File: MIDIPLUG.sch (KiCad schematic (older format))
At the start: 33 parts, among them P1 LINE OUT, U1 LP2985-3.3, U2 SAM2695, Y1 12Mhz

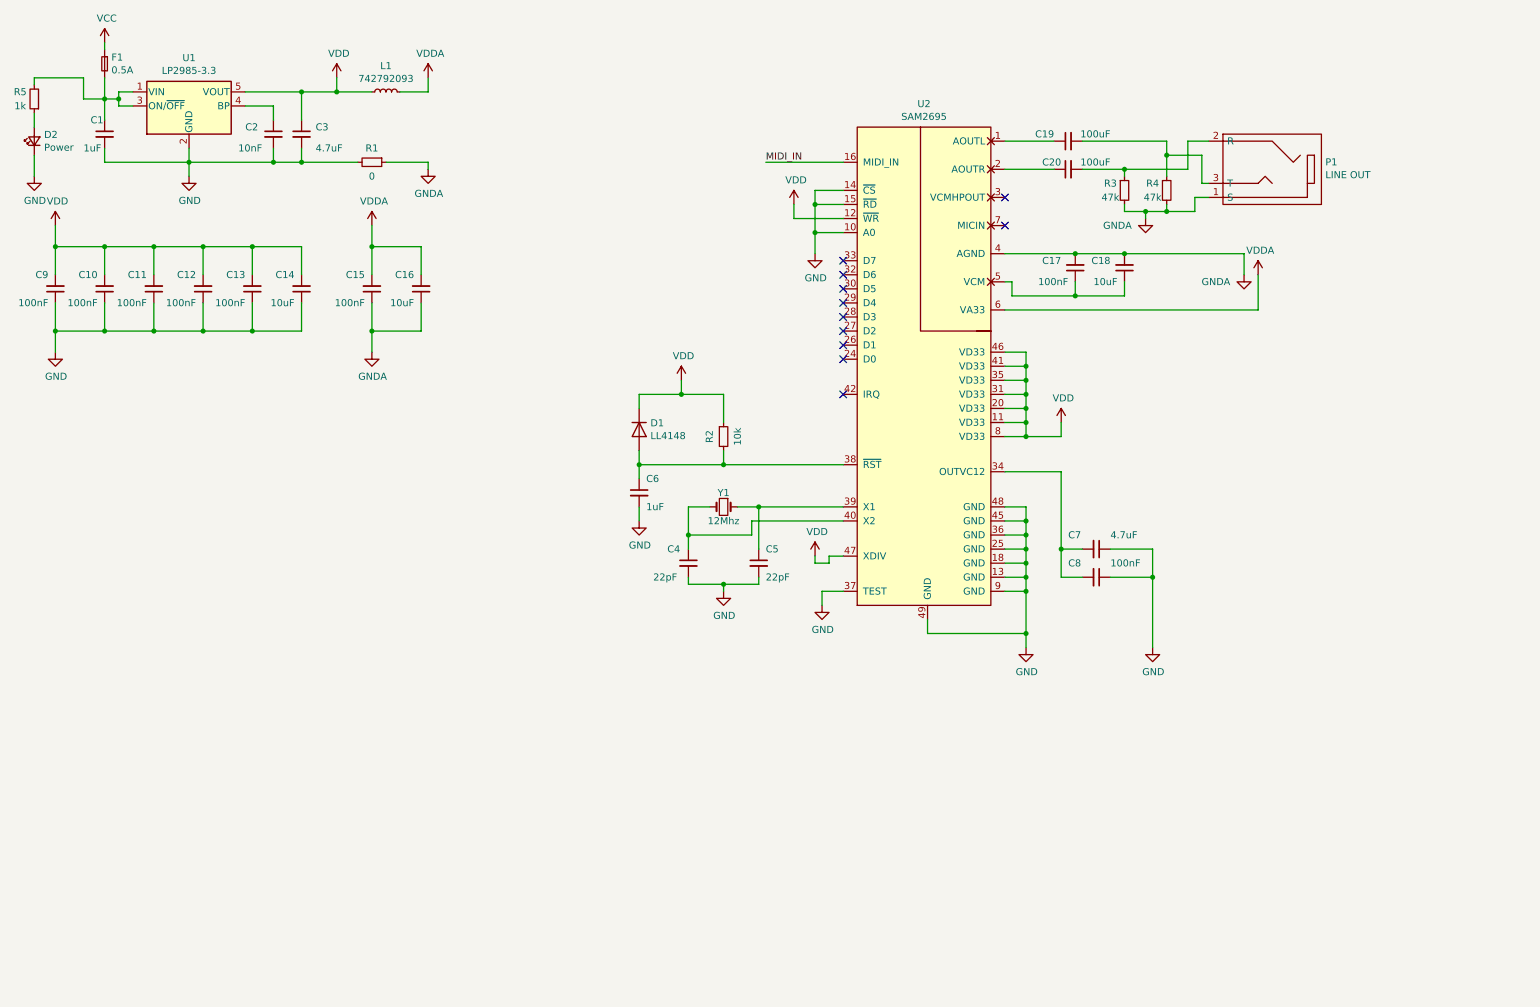
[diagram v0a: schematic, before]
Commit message: Add joystick plug
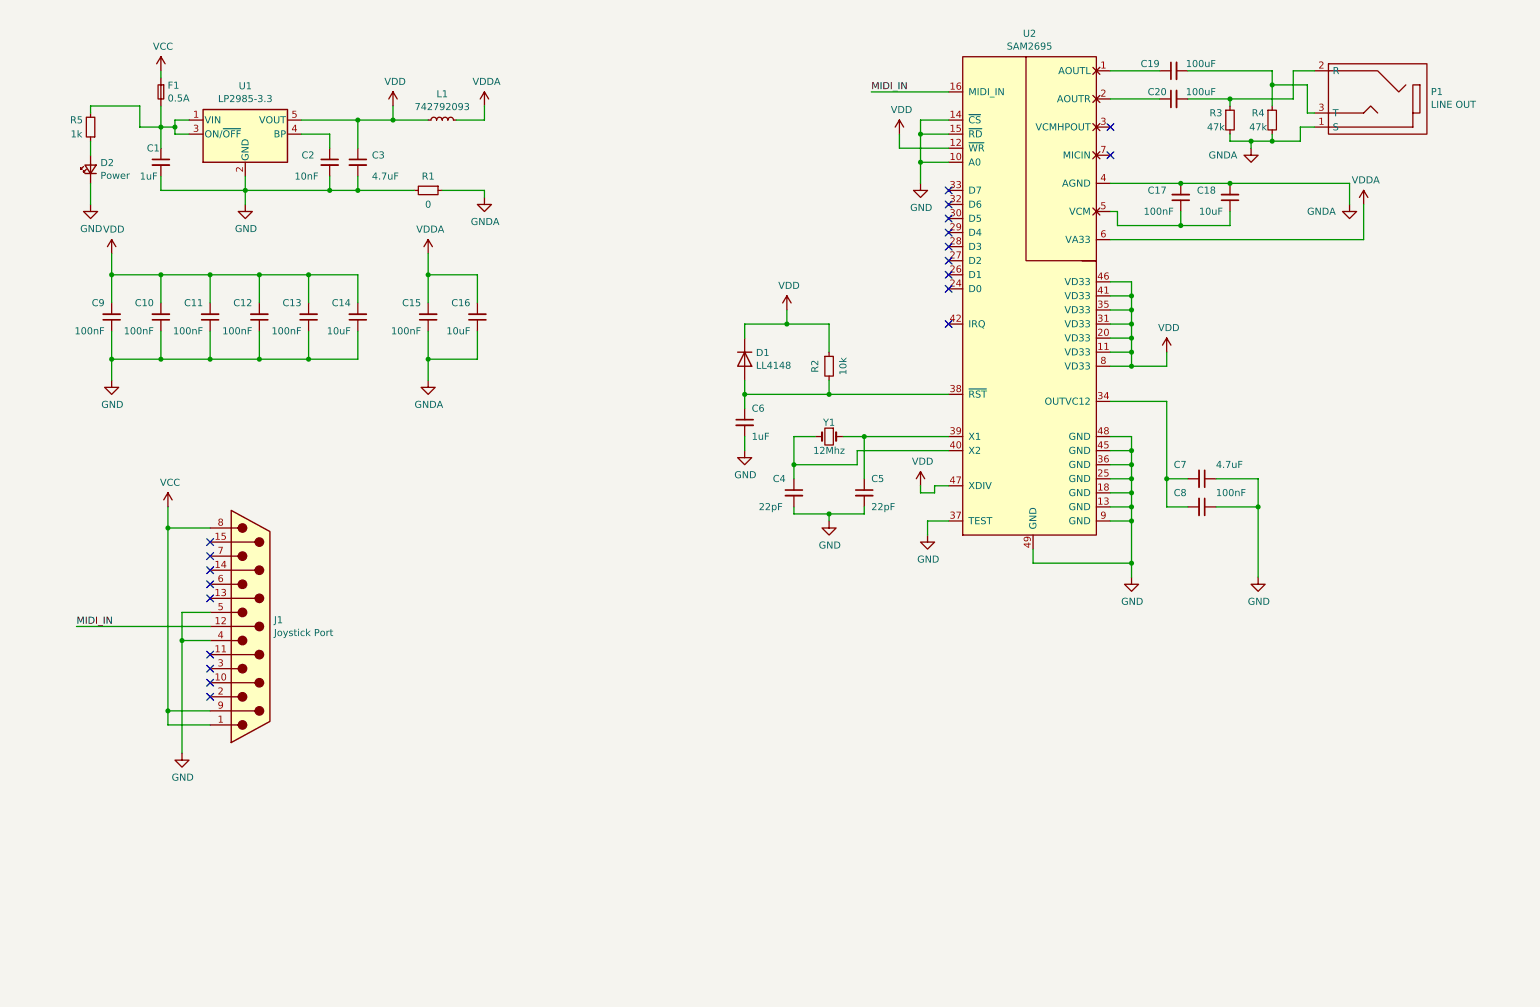
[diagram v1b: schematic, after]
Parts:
- added J1: Joystick Port, symbol Connector:DB15_Male
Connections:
- net GND: now also J1.4, J1.5
- net MIDI_IN: now also J1.12 (P12)
- net VCC: now also J1.1, J1.8, J1.9 (P9)
- no-connect marks 11 -> 20
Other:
- moved on the sheet: C1, C10, C11, C12, C13, C14, C15, C16, C17, C18, C19, C2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

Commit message: Begin placing components
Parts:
- C1: footprint (none) -> Capacitor_SMD:C_0805_2012Metric_Pad1.18x1.45mm_HandSolder
- C19, C20: footprint (none) -> Capacitor_SMD:C_1206_3216Metric_Pad1.33x1.80mm_HandSolder
- D2: footprint (none) -> LED_SMD:LED_1206_3216Metric_Pad1.42x1.75mm_HandSolder
- F1: footprint (none) -> Fuse:Fuse_1206_3216Metric_Pad1.42x1.75mm_HandSolder
- J1: footprint (none) -> Connector_Dsub:DSUB-15_Male_EdgeMount_P2.77mm
- L1: footprint (none) -> Inductor_SMD:L_0805_2012Metric_Pad1.15x1.40mm_HandSolder
- P1: footprint (none) -> My_Components:Conn_Audio_3.5mm_Stereo_SJ1-352XNG
- R1, R2, R3, R4, R5: footprint (none) -> Resistor_SMD:R_0805_2012Metric_Pad1.20x1.40mm_HandSolder
- U2: footprint (none) -> Package_DFN_QFN:QFN-48-1EP_6x6mm_P0.4mm_EP4.3x4.3mm_ThermalVias
- Y1: footprint (none) -> Crystal:Crystal_SMD_HC49-SD

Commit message: First version of the PCB
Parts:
- removed C11, C12, C13: 100nF, symbol Device:C_Small
- C10, C14, C15, C16, C17, C18, C2, C3, C4, C5, C6, C7, C8, C9: footprint (none) -> Capacitor_SMD:C_0805_2012Metric_Pad1.18x1.45mm_HandSolder
- D2: footprint LED_SMD:LED_1206_3216Metric_Pad1.42x1.75mm_HandSolder -> LED_SMD:LED_0805_2012Metric_Pad1.15x1.40mm_HandSolder
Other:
- moved on the sheet: C14, C4, C5
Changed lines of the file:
@@
 F 0 "C2" H 2600 1800 50  0000 L CNN
 F 1 "10nF" H 2550 1650 50  0000 L CNN
-F 2 "" H 2800 1750 50  0001 C CNN
+F 2 "Capacitor_SMD:C_0805_2012Metric_Pad1.18x1.45mm_HandSolder" H 2800 1750 50  0001 C CNN
 F 3 "~" H 2800 1750 50  0001 C CNN
 	1    2800 1750
@@
 F 0 "C3" H 3100 1800 50  0000 L CNN
 F 1 "4.7uF" H 3100 1650 50  0000 L CNN
-F 2 "" H 3000 1750 50  0001 C CNN
+F 2 "Capacitor_SMD:C_0805_2012Metric_Pad1.18x1.45mm_HandSolder" H 3000 1750 50  0001 C CNN
 F 3 "~" H 3000 1750 50  0001 C CNN
 	1    3000 1750
@@
 	8500 4700 8500 4600
 Connection ~ 8500 4600
-$Comp
-L Device:Crystal_Small Y1
-U 1 1 60B4BC85
-P 6350 3700
-F 0 "Y1" H 6350 3600 50  0000 C CNN
-F 1 "12Mhz" H 6350 3800 50  0000 C CNN
-F 2 "Crystal:Crystal_SMD_HC49-SD" H 6350 3700 50  0001 C CNN
-F 3 "~" H 6350 3700 50  0001 C CNN
-	1    6350 3700
-	-1   0    0    1
-$EndComp
-$Comp
-L Device:C_Small C4
-U 1 1 60B4CDD2
-P 6100 4100
-F 0 "C4" H 5950 4200 50  0000 L CNN
-F 1 "22pF" H 5850 4000 50  0000 L CNN
-F 2 "" H 6100 4100 50  0001 C CNN
-F 3 "~" H 6100 4100 50  0001 C CNN
-	1    6100 4100
-	1    0    0    -1
-$EndComp
-$Comp
-L Device:C_Small C5
-U 1 1 60B4E9FB
-P 6600 4100
-F 0 "C5" H 6650 4200 50  0000 L CNN
-F 1 "22pF" H 6650 4000 50  0000 L CNN
-F 2 "" H 6600 4100 50  0001 C CNN
-F 3 "~" H 6600 4100 50  0001 C CNN
-	1    6600 4100
-	1    0    0    -1
-$EndComp
 Wire Wire Line
 	7200 1750 7000 1750
@@
 F 0 "C6" H 5800 3700 50  0000 L CNN
 F 1 "1uF" H 5800 3500 50  0000 L CNN
-F 2 "" H 5750 3600 50  0001 C CNN
+F 2 "Capacitor_SMD:C_0805_2012Metric_Pad1.18x1.45mm_HandSolder" H 5750 3600 50  0001 C CNN
 F 3 "~" H 5750 3600 50  0001 C CNN
 	1    5750 3600
@@
 F 0 "C7" V 8900 3800 50  0000 L CNN
 F 1 "4.7uF" V 8900 4100 50  0000 L CNN
-F 2 "" H 9000 4000 50  0001 C CNN
+F 2 "Capacitor_SMD:C_0805_2012Metric_Pad1.18x1.45mm_HandSolder" H 9000 4000 50  0001 C CNN
 F 3 "~" H 9000 4000 50  0001 C CNN
 	1    9000 4000
@@
 F 0 "C8" V 8900 4000 50  0000 L CNN
 F 1 "100nF" V 8900 4300 50  0000 L CNN
-F 2 "" H 9000 4200 50  0001 C CNN
+F 2 "Capacitor_SMD:C_0805_2012Metric_Pad1.18x1.45mm_HandSolder" H 9000 4200 50  0001 C CNN
 F 3 "~" H 9000 4200 50  0001 C CNN
 	1    9000 4200
@@
 F 0 "C9" H 1300 2750 50  0000 L CNN
 F 1 "100nF" H 1300 2950 50  0000 L CNN
-F 2 "" H 1250 2850 50  0001 C CNN
+F 2 "Capacitor_SMD:C_0805_2012Metric_Pad1.18x1.45mm_HandSolder" H 1250 2850 50  0001 C CNN
 F 3 "~" H 1250 2850 50  0001 C CNN
 	1    1250 2850
@@
 F 0 "C10" H 1650 2750 50  0000 L CNN
 F 1 "100nF" H 1650 2950 50  0000 L CNN
-F 2 "" H 1600 2850 50  0001 C CNN
+F 2 "Capacitor_SMD:C_0805_2012Metric_Pad1.18x1.45mm_HandSolder" H 1600 2850 50  0001 C CNN
 F 3 "~" H 1600 2850 50  0001 C CNN
 	1    1600 2850
@@
 $EndComp
 $Comp
-L Device:C_Small C11
-U 1 1 60B93414
+L Device:C_Small C14
+U 1 1 60B967FC
 P 1950 2850
-F 0 "C11" H 2000 2750 50  0000 L CNN
-F 1 "100nF" H 2000 2950 50  0000 L CNN
-F 2 "" H 1950 2850 50  0001 C CNN
+F 0 "C14" H 2000 2750 50  0000 L CNN
+F 1 "10uF" H 2000 2950 50  0000 L CNN
+F 2 "Capacitor_SMD:C_0805_2012Metric_Pad1.18x1.45mm_HandSolder" H 1950 2850 50  0001 C CNN
 F 3 "~" H 1950 2850 50  0001 C CNN
 	1    1950 2850
 	-1   0    0    1
 $EndComp
-$Comp
-L Device:C_Small C12
-U 1 1 60B96526
-P 2300 2850
-F 0 "C12" H 2350 2750 50  0000 L CNN
-F 1 "100nF" H 2350 2950 50  0000 L CNN
-F 2 "" H 2300 2850 50  0001 C CNN
-F 3 "~" H 2300 2850 50  0001 C CNN
-	1    2300 2850
-	-1   0    0    1
-$EndComp
-$Comp
-L Device:C_Small C13
-U 1 1 60B967F2
-P 2650 2850
-F 0 "C13" H 2700 2750 50  0000 L CNN
-F 1 "100nF" H 2700 2950 50  0000 L CNN
-F 2 "" H 2650 2850 50  0001 C CNN
-F 3 "~" H 2650 2850 50  0001 C CNN
-	1    2650 2850
-	-1   0    0    1
-$EndComp
-$Comp
-L Device:C_Small C14
-U 1 1 60B967FC
-P 3000 2850
-F 0 "C14" H 3050 2750 50  0000 L CNN
-F 1 "10uF" H 3050 2950 50  0000 L CNN
-F 2 "" H 3000 2850 50  0001 C CNN
-F 3 "~" H 3000 2850 50  0001 C CNN
-	1    3000 2850
-	-1   0    0    1
-$EndComp
 Wire Wire Line
 	1250 2950 1250 3150
@@
 	1250 3150 1600 3150
 Wire Wire Line
-	3000 3150 3000 2950
-Wire Wire Line
-	2650 2950 2650 3150
-Connection ~ 2650 3150
-Wire Wire Line
-	2650 3150 3000 3150
-Wire Wire Line
-	2300 2950 2300 3150
-Connection ~ 2300 3150
-Wire Wire Line
-	2300 3150 2650 3150
-Wire Wire Line
 	1950 2950 1950 3150
-Connection ~ 1950 3150
-Wire Wire Line
-	1950 3150 2300 3150
 Wire Wire Line
 	1600 2950 1600 3150
@@
 	1250 2550 1600 2550
 Wire Wire Line
-	3000 2550 3000 2750
-Wire Wire Line
-	2650 2750 2650 2550
-Connection ~ 2650 2550
-Wire Wire Line
-	2650 2550 3000 2550
-Wire Wire Line
-	2300 2750 2300 2550
-Connection ~ 2300 2550
-Wire Wire Line
-	2300 2550 2650 2550
-Wire Wire Line
 	1950 2750 1950 2550
-Connection ~ 1950 2550
-Wire Wire Line
-	1950 2550 2300 2550
 Wire Wire Line
 	1600 2750 1600 2550
@@
 F 0 "C15" H 3550 2750 50  0000 L CNN
 F 1 "100nF" H 3550 2950 50  0000 L CNN
-F 2 "" H 3500 2850 50  0001 C CNN
+F 2 "Capacitor_SMD:C_0805_2012Metric_Pad1.18x1.45mm_HandSolder" H 3500 2850 50  0001 C CNN
 F 3 "~" H 3500 2850 50  0001 C CNN
 	1    3500 2850
@@
 F 0 "C16" H 3900 2750 50  0000 L CNN
 F 1 "10uF" H 3900 2950 50  0000 L CNN
-F 2 "" H 3850 2850 50  0001 C CNN
+F 2 "Capacitor_SMD:C_0805_2012Metric_Pad1.18x1.45mm_HandSolder" H 3850 2850 50  0001 C CNN
 F 3 "~" H 3850 2850 50  0001 C CNN
 	1    3850 2850
@@
 F 0 "C17" H 8950 1950 50  0000 L CNN
 F 1 "100nF" H 8900 2100 50  0000 L CNN
-F 2 "" H 8850 2000 50  0001 C CNN
+F 2 "Capacitor_SMD:C_0805_2012Metric_Pad1.18x1.45mm_HandSolder" H 8850 2000 50  0001 C CNN
 F 3 "~" H 8850 2000 50  0001 C CNN
 	1    8850 2000
@@
 F 0 "C18" H 9300 1950 50  0000 L CNN
 F 1 "10uF" H 9250 2100 50  0000 L CNN
-F 2 "" H 9200 2000 50  0001 C CNN
+F 2 "Capacitor_SMD:C_0805_2012Metric_Pad1.18x1.45mm_HandSolder" H 9200 2000 50  0001 C CNN
 F 3 "~" H 9200 2000 50  0001 C CNN
 	1    9200 2000
@@
 F 0 "D2" V 1146 1730 50  0000 R CNN
 F 1 "Power" V 1055 1730 50  0000 R CNN
-F 2 "LED_SMD:LED_1206_3216Metric_Pad1.42x1.75mm_HandSolder" V 1100 1800 50  0001 C CNN
+F 2 "LED_SMD:LED_0805_2012Metric_Pad1.15x1.40mm_HandSolder" V 1100 1800 50  0001 C CNN
 F 3 "~" V 1100 1800 50  0001 C CNN
 	1    1100 1800
@@
 NoConn ~ 1950 5450
 NoConn ~ 1950 5550
+$Comp
+L Device:C_Small C5
+U 1 1 60B4E9FB
+P 6100 4100
+F 0 "C5" H 6150 4200 50  0000 L CNN
+F 1 "22pF" H 6150 4000 50  0000 L CNN
+F 2 "Capacitor_SMD:C_0805_2012Metric_Pad1.18x1.45mm_HandSolder" H 6100 4100 50  0001 C CNN
+F 3 "~" H 6100 4100 50  0001 C CNN
+	1    6100 4100
+	1    0    0    -1
+$EndComp
+$Comp
+L Device:C_Small C4
+U 1 1 60B4CDD2
+P 6600 4100
+F 0 "C4" H 6450 4200 50  0000 L CNN
+F 1 "22pF" H 6350 4000 50  0000 L CNN
+F 2 "Capacitor_SMD:C_0805_2012Metric_Pad1.18x1.45mm_HandSolder" H 6600 4100 50  0001 C CNN
+F 3 "~" H 6600 4100 50  0001 C CNN
+	1    6600 4100
+	1    0    0    -1
+$EndComp
+$Comp
+L Device:Crystal_Small Y1
+U 1 1 60B4BC85
+P 6350 3700
+F 0 "Y1" H 6350 3600 50  0000 C CNN
+F 1 "12Mhz" H 6350 3800 50  0000 C CNN
+F 2 "Crystal:Crystal_SMD_HC49-SD" H 6350 3700 50  0001 C CNN
+F 3 "~" H 6350 3700 50  0001 C CNN
+	1    6350 3700
+	1    0    0    -1
+$EndComp
+Connection ~ 1950 2550
+Connection ~ 1950 3150
+Wire Wire Line
+	1950 2550 2300 2550
+Connection ~ 2300 2550
+Wire Wire Line
+	2300 2750 2300 2550
+Wire Wire Line
+	2300 2550 2650 2550
+Wire Wire Line
+	2650 2550 3000 2550
+Connection ~ 2650 2550
+Wire Wire Line
+	2650 2750 2650 2550
+Wire Wire Line
+	3000 2550 3000 2750
+Wire Wire Line
+	1950 3150 2300 3150
+Connection ~ 2300 3150
+Wire Wire Line
+	2300 2950 2300 3150
+Wire Wire Line
+	2300 3150 2650 3150
+Wire Wire Line
+	2650 3150 3000 3150
+Connection ~ 2650 3150
+Wire Wire Line
+	2650 2950 2650 3150
+Wire Wire Line
+	3000 3150 3000 2950
 $EndSCHEMATC

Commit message: Tweak silkscreen
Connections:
- wire segments 191 -> 179
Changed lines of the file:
@@
 encoding utf-8
 Sheet 1 1
-Title ""
+Title "MIDI-STICK"
 Date ""
-Rev ""
+Rev "0.1"
 Comp ""
 Comment1 ""
@@
 F 0 "P1" H 9872 1351 50  0000 R CNN
 F 1 "LINE OUT" H 9872 1260 50  0000 R CNN
-F 2 "My_Components:Conn_Audio_3.5mm_Stereo_SJ1-352XNG" H 10400 1450 50  0000 C CNN
+F 2 "My_Components:Conn_Audio_3.5mm_Stereo_SJ1-352XNG" H 10400 1450 50  0001 C CNN
 F 3 "" H 10400 1450 50  0000 C CNN
 	1    10250 1300
@@
 	1    0    0    -1
 $EndComp
-Connection ~ 1950 2550
-Connection ~ 1950 3150
-Wire Wire Line
-	1950 2550 2300 2550
-Connection ~ 2300 2550
-Wire Wire Line
-	2300 2750 2300 2550
-Wire Wire Line
-	2300 2550 2650 2550
-Wire Wire Line
-	2650 2550 3000 2550
-Connection ~ 2650 2550
-Wire Wire Line
-	2650 2750 2650 2550
-Wire Wire Line
-	3000 2550 3000 2750
-Wire Wire Line
-	1950 3150 2300 3150
-Connection ~ 2300 3150
-Wire Wire Line
-	2300 2950 2300 3150
-Wire Wire Line
-	2300 3150 2650 3150
-Wire Wire Line
-	2650 3150 3000 3150
-Connection ~ 2650 3150
-Wire Wire Line
-	2650 2950 2650 3150
-Wire Wire Line
-	3000 3150 3000 2950
 $EndSCHEMATC

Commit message: Add hole on underside of SAM chip
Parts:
- U2: footprint Package_DFN_QFN:QFN-48-1EP_6x6mm_P0.4mm_EP4.3x4.3mm_ThermalVias -> MIDIPLUG:QFN-48-1EP_6x6mm_P0.4mm_EP4.66x4.66mm_BackHoles
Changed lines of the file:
@@
 F 0 "U2" H 7775 4065 50  0000 C CNN
 F 1 "SAM2695" H 7775 3974 50  0000 C CNN
-F 2 "Package_DFN_QFN:QFN-48-1EP_6x6mm_P0.4mm_EP4.3x4.3mm_ThermalVias" H 7350 3950 50  0001 C CNN
+F 2 "MIDIPLUG:QFN-48-1EP_6x6mm_P0.4mm_EP4.66x4.66mm_BackHoles" H 7350 3950 50  0001 C CNN
 F 3 "" H 7350 3950 50  0001 C CNN
 	1    7750 2450

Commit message: Rewrite the schematics to support waveblaster
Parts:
- removed D1: LL4148, Diode_SMD:D_MiniMELF, symbol Diode:LL4148
- removed D2: Power, LED_SMD:LED_0805_2012Metric_Pad1.15x1.40mm_HandSolder, symbol Device:LED_Small
- removed J1: Joystick Port, Connector_Dsub:DSUB-15_Male_EdgeMount_P2.77mm, symbol Connector:DB15_Male
- removed P1: LINE OUT, My_Components:Conn_Audio_3.5mm_Stereo_SJ1-352XNG, symbol my_components:JACK_TRS_3PINS
- removed R2: 10k, Resistor_SMD:R_0805_2012Metric_Pad1.20x1.40mm_HandSolder, symbol Device:R_Small
- removed R5: 1k, Resistor_SMD:R_0805_2012Metric_Pad1.20x1.40mm_HandSolder, symbol Device:R_Small
- added J1: Wavetable Connector, Connector_PinSocket_2.54mm:PinSocket_2x13_P2.54mm_Vertical, symbol Connector_Generic:Conn_02x13_Odd_Even
- added U3: 4050, symbol 4xxx:4050
- Y1: footprint Crystal:Crystal_SMD_HC49-SD -> Crystal:Crystal_AT310_D3.0mm_L10.0mm_Horizontal_1EP_style2; symbol Device:Crystal_Small -> Device:Crystal_GND3_Small
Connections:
- net GND: now also Y1.3, J1.1 (Pin_1), J1.11 (Pin_11), J1.3 (Pin_3), J1.5 (Pin_5), J1.7 (Pin_7), J1.9 (Pin_9), U3.11, U3.14, U3.7, U3.8 (VSS), U3.9
- net MIDI_IN: now also J1.4 (Pin_4), U3.5; no longer U2.16 (MIDI_IN)
- net VCC: now also J1.10 (Pin_10), J1.14 (Pin_14), J1.6 (Pin_6)
- net VDD: now also U3.1 (VCC)
- net at C6.1, U2.38 (~RST): now also U3.2
- net AOUT_L: now reaches C19.2, R4.1
- net AOUT_L: now also J1.24 (Pin_24)
- net AOUT_R: now reaches C20.2, R3.1
- net AOUT_R: now also J1.20 (Pin_20)
- new net: U2.16 (MIDI_IN), U3.4
- new net ~RESET_5V: J1.26 (Pin_26), U3.3
- no-connect marks 20 -> 28
